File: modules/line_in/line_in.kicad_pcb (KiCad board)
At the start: 2 copper layers, 30.5 x 68.6 mm, 4 parts

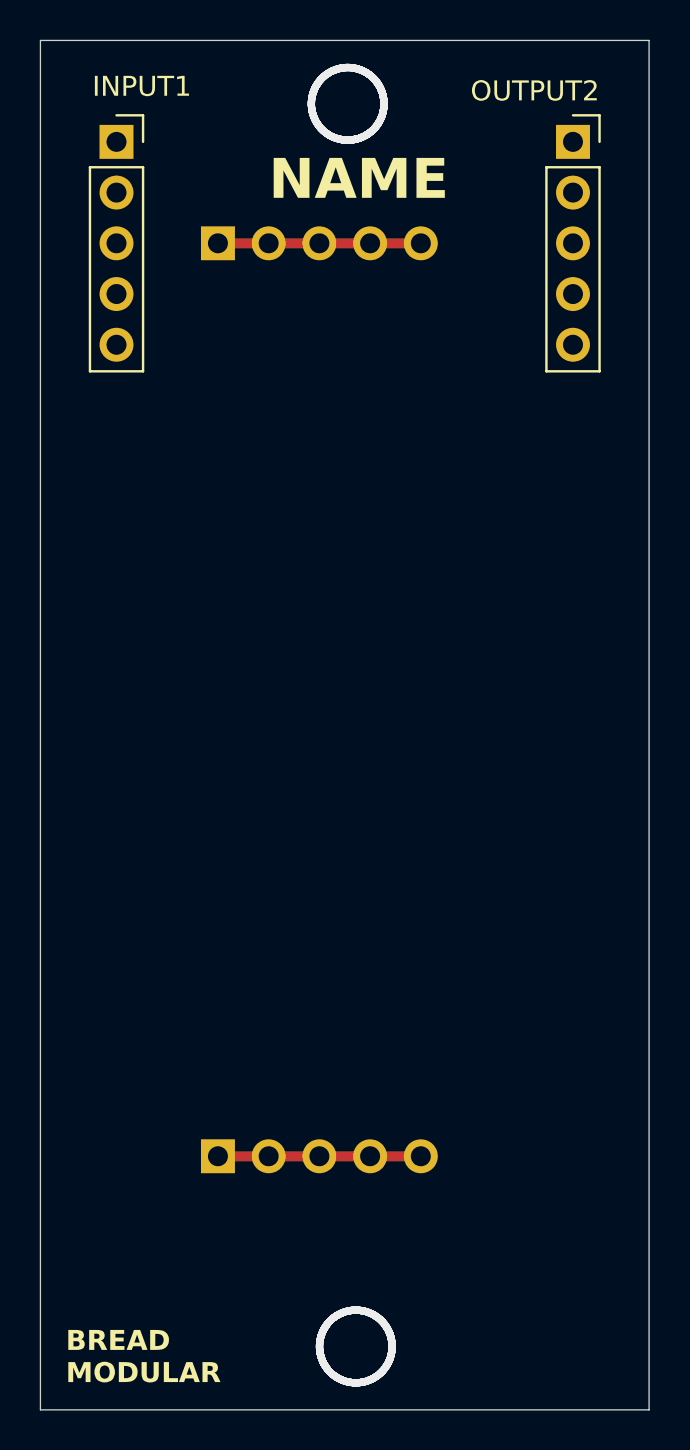
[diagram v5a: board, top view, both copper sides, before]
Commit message: Finished building the line_in module.
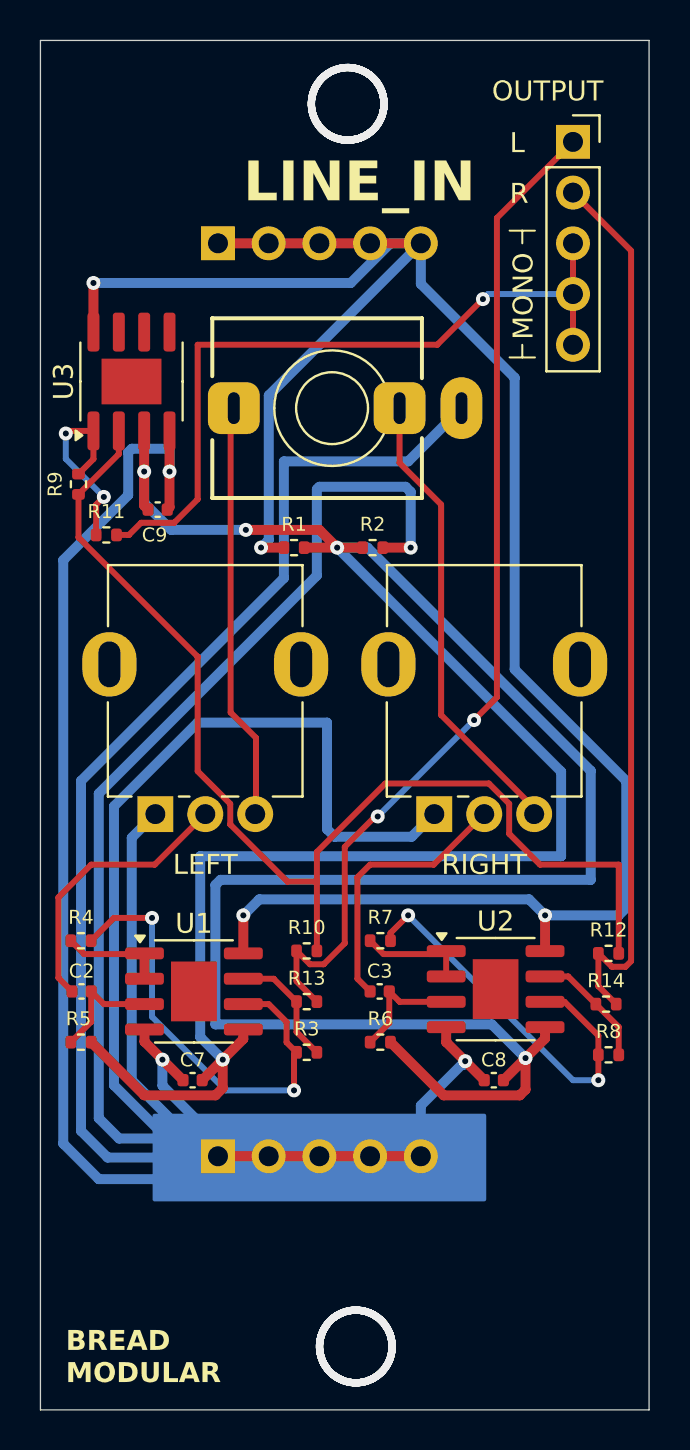
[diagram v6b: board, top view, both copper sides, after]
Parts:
- removed INPUT1: Conn_01x05_Socket, Connector_PinSocket_2.54mm:PinSocket_1x05_P2.54mm_Vertical
- added C2: 0.1uf, Capacitor_SMD:C_0402_1005Metric, F.Cu at (49.0, 88.3)
- added C3: 0.1uf, Capacitor_SMD:C_0402_1005Metric, F.Cu at (64.0, 88.3)
- added C7: 0.1uf, Capacitor_SMD:C_0402_1005Metric, F.Cu at (54.6, 92.7)
- added C8: 0.1uf, Capacitor_SMD:C_0402_1005Metric, F.Cu at (69.7, 92.7)
- added C9: 0.1uf, Capacitor_SMD:C_0402_1005Metric, F.Cu at (52.9, 64.1)
- added J1: AudioJack3, BreadModular_AudioJacks:Jack_3.5mm_QingPu_WQP-PJ366ST_Vertical, F.Cu at (61.6, 59.1)
- added LEFT: 50k, BreadModular_Pots:Potentiometer_RV09, F.Cu at (52.7, 79.4)
- added R1: 1k, Resistor_SMD:R_0402_1005Metric, F.Cu at (59.7, 66.0)
- added R10: 100k, Resistor_SMD:R_0402_1005Metric, F.Cu at (60.3, 86.2)
- added R11: 1k, Resistor_SMD:R_0402_1005Metric, F.Cu at (50.3, 65.4)
- added R12: 100k, Resistor_SMD:R_0402_1005Metric, F.Cu at (75.4, 86.4)
- added R13: 1k, Resistor_SMD:R_0402_1005Metric, F.Cu at (60.3, 88.8)
- added R14: 1k, Resistor_SMD:R_0402_1005Metric, F.Cu at (75.3, 88.9)
- added R2: 1k, Resistor_SMD:R_0402_1005Metric, F.Cu at (63.6, 66.0)
- added R3: 100k, Resistor_SMD:R_0402_1005Metric, F.Cu at (60.3, 91.3)
- added R4: 24k, Resistor_SMD:R_0402_1005Metric, F.Cu at (49.0, 85.7)
- added R5: 100k, Resistor_SMD:R_0402_1005Metric, F.Cu at (49.0, 90.8)
- added R6: 100k, Resistor_SMD:R_0402_1005Metric, F.Cu at (64.0, 90.8)
- added R7: 24k, Resistor_SMD:R_0402_1005Metric, F.Cu at (64.0, 85.7)
- added R8: 100k, Resistor_SMD:R_0402_1005Metric, F.Cu at (75.4, 91.4)
- added R9: 50k, Resistor_SMD:R_0402_1005Metric, F.Cu at (48.9, 62.9)
- added RIGHT: 50k, BreadModular_Pots:Potentiometer_RV09, F.Cu at (66.7, 79.4)
- added U1: TL072, Package_SO:SOIC-8-1EP_3.9x4.9mm_P1.27mm_EP2.29x3mm, F.Cu at (54.7, 88.3)
- added U2: TL072, Package_SO:SOIC-8-1EP_3.9x4.9mm_P1.27mm_EP2.29x3mm, F.Cu at (69.8, 88.2)
- added U3: TL072, Package_SO:SOIC-8-1EP_3.9x4.9mm_P1.27mm_EP2.29x3mm, F.Cu at (51.5, 57.7)
- renumbered OUTPUT2 to OUTPUT
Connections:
- net Net-(5V1-Pin_1) renamed +5V
- OUTPUT pad 1: unconnected-(OUTPUT2-Pin_1-Pad1) -> OUT_L
- OUTPUT pad 2: unconnected-(OUTPUT2-Pin_2-Pad2) -> OUT_R
- OUTPUT pad 3: unconnected-(OUTPUT2-Pin_3-Pad3) -> OUT_MONO
- OUTPUT pad 4: unconnected-(OUTPUT2-Pin_4-Pad4) -> OUT_MONO
- OUTPUT pad 5: unconnected-(OUTPUT2-Pin_5-Pad5) -> OUT_MONO
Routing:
- net GND: track 10.2 -> 251.7 mm, vias 0 -> 4
- net 2.5V: track 0.00 -> 158.6 mm, vias 0 -> 5
- net +5V: track 10.2 -> 110.8 mm, vias 0 -> 4
- net Net-(U3A--): track 0.00 -> 57.7 mm
- net OUT_L: track 0.00 -> 51.0 mm, vias 0 -> 2
- net OUT_R: track 0.00 -> 44.7 mm
- net OUT_MONO: track 0.00 -> 37.6 mm, vias 0 -> 1
- net Net-(U1B--): track 0.00 -> 23.3 mm, vias 0 -> 2
- net IN_R: track 0.00 -> 23.1 mm
- net IN_L: track 0.00 -> 20.9 mm
- net Net-(U2B--): track 0.00 -> 20.2 mm, vias 0 -> 2
- net Net-(C2-Pad1): track 0.00 -> 14.1 mm
- net Net-(C3-Pad1): track 0.00 -> 13.6 mm
- net Net-(R11-Pad1): track 0.00 -> 9.94 mm, vias 0 -> 2
- net Net-(R14-Pad1): track 0.00 -> 6.13 mm
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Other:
- board text added: "L"
- board text added: "LINE_IN"
- board text added: "MONO"
- board text added: "R"
- board text removed: "NAME"

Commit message: Add the line_in 0.3.0 production build
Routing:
- net Net-(U3A--): track 57.7 -> 58.3 mm
- net IN_L: track 20.9 -> 21.0 mm, vias 0 -> 1
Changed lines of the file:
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@@
 	)
 	(segment
-		(start 57.785 75.565)
-		(end 57.785 79.345)
-		(width 0.3)
-		(layer "F.Cu")
-		(net 10)
-	)
-	(segment
-		(start 56.515 74.295)
-		(end 57.785 75.565)
+		(start 56.515 74.041)
+		(end 56.515 76.073)
 		(width 0.3)
 		(layer "F.Cu")
@@
 	(segment
 		(start 56.515 59.215)
-		(end 56.515 74.295)
+		(end 56.515 74.041)
 		(width 0.3)
 		(layer "F.Cu")
@@
 		(net 10)
 	)
+	(via
+		(at 56.515 76.073)
+		(size 0.7)
+		(drill 0.3)
+		(layers "F.Cu" "B.Cu")
+		(net 10)
+	)
+	(segment
+		(start 56.515 78.155)
+		(end 57.745 79.385)
+		(width 0.3)
+		(layer "B.Cu")
+		(net 10)
+	)
+	(segment
+		(start 56.515 76.073)
+		(end 56.515 78.155)
+		(width 0.3)
+		(layer "B.Cu")
+		(net 10)
+	)
 	(segment
 		(start 76.57 51.17)
@@
 	)
 	(segment
-		(start 59.357233 82.765)
-		(end 60.835 82.765)
-		(width 0.3)
-		(layer "F.Cu")
-		(net 17)
-	)
-	(segment
 		(start 60.835 86.235)
 		(end 60.835 82.765)
@@
 	)
 	(segment
+		(start 59.944 80.387)
+		(end 59.944 77.089)
+		(width 0.5)
+		(layer "F.Cu")
+		(net 17)
+	)
+	(segment
 		(start 60.835 81.278)
 		(end 64.262 77.851)
@@
 	)
 	(segment
-		(start 54.864 71.498634)
-		(end 54.864 77.236233)
-		(width 0.3)
+		(start 48.895 65.671056)
+		(end 48.895 63.375)
+		(width 0.5)
 		(layer "F.Cu")
 		(net 17)
@@
 	)
 	(segment
-		(start 56.495 78.867233)
-		(end 56.495 79.902767)
-		(width 0.3)
-		(layer "F.Cu")
-		(net 17)
-	)
-	(segment
-		(start 54.864 77.236233)
-		(end 56.495 78.867233)
-		(width 0.3)
+		(start 54.61 70.866)
+		(end 49.919 66.175)
+		(width 0.5)
+		(layer "F.Cu")
+		(net 17)
+	)
+	(segment
+		(start 60.835 81.278)
+		(end 59.944 80.387)
+		(width 0.5)
+		(layer "F.Cu")
+		(net 17)
+	)
+	(segment
+		(start 55.372 77.089)
+		(end 54.61 76.327)
+		(width 0.5)
 		(layer "F.Cu")
 		(net 17)
@@
 	)
 	(segment
-		(start 48.895 65.529634)
-		(end 54.864 71.498634)
-		(width 0.3)
-		(layer "F.Cu")
-		(net 17)
-	)
-	(segment
-		(start 56.495 79.902767)
-		(end 59.357233 82.765)
-		(width 0.3)
+		(start 49.398944 66.175)
+		(end 48.895 65.671056)
+		(width 0.5)
+		(layer "F.Cu")
+		(net 17)
+	)
+	(segment
+		(start 49.919 66.175)
+		(end 49.398944 66.175)
+		(width 0.5)
 		(layer "F.Cu")
 		(net 17)
@@
 	)
 	(segment
-		(start 48.895 63.375)
-		(end 48.895 65.529634)
-		(width 0.3)
+		(start 54.61 76.327)
+		(end 54.61 70.866)
+		(width 0.5)
 		(layer "F.Cu")
 		(net 17)
@@
 		(layer "F.Cu")
 		(net 17)
+	)
+	(segment
+		(start 59.944 77.089)
+		(end 55.372 77.089)
+		(width 0.5)
+		(layer "F.Cu")
+		(net 17)

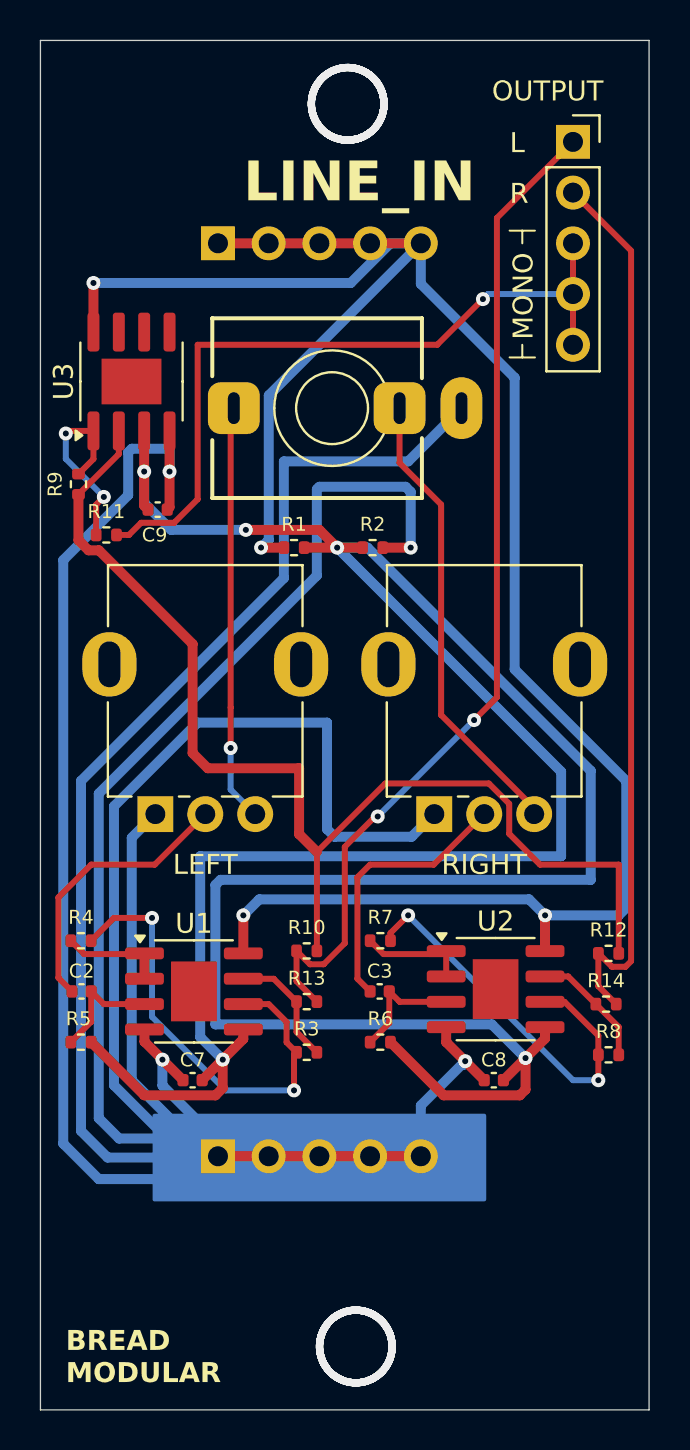
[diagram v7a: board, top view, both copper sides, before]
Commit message: Update line_in to use MCP6001 and 3V3.
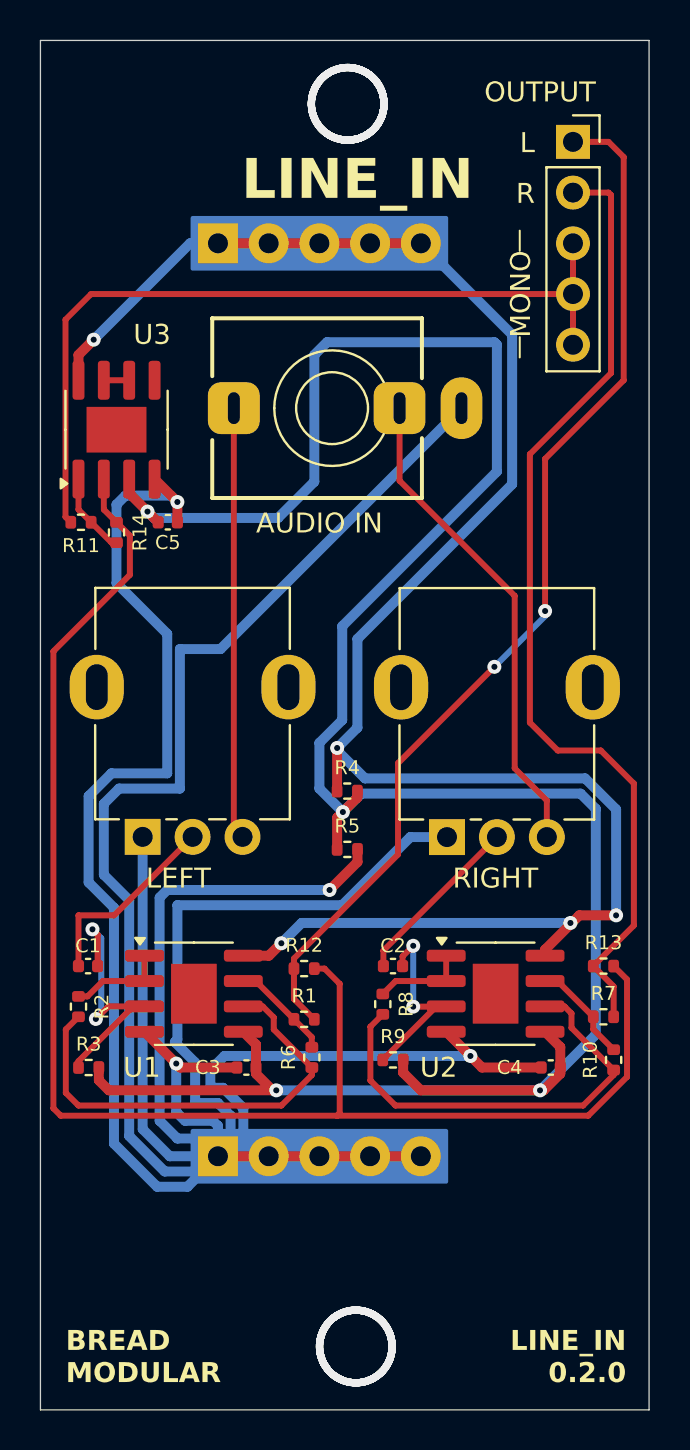
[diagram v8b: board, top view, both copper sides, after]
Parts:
- removed 5V1: Conn_01x05_Pin, Connector_PinHeader_2.54mm:PinHeader_1x05_P2.54mm_Vertical
- removed C7, C8, C9: 0.1uf, Capacitor_SMD:C_0402_1005Metric
- removed LEFT, RIGHT: 50k, BreadModular_Pots:Potentiometer_RV09
- removed OUTPUT: Conn_01x05_Socket, Connector_PinSocket_2.54mm:PinSocket_1x05_P2.54mm_Vertical
- added C1: 0.1uf, Capacitor_SMD:C_0402_1005Metric, F.Cu at (49.4, 87.0)
- added C4: 0.1uf, Capacitor_SMD:C_0402_1005Metric, F.Cu at (72.5, 92.1)
- added C5: 0.1uf, Capacitor_SMD:C_0402_1005Metric, F.Cu at (53.4, 64.8)
- added OUTPUT1: Conn_01x05_Socket, Connector_PinSocket_2.54mm:PinSocket_1x05_P2.54mm_Vertical, F.Cu at (73.7, 45.7)
- added RV1: 50k, BreadModular_Pots:Potentiometer_RV09, F.Cu at (52.1, 80.5)
- added RV2: 50k, BreadModular_Pots:Potentiometer_RV09, F.Cu at (67.3, 80.5)
- added VSUPPLY1: Conn_01x05_Pin, BreadModular_MISC:Power_Connector, B.Cu at (55.9, 50.8)
- GND1: footprint Connector_PinHeader_2.54mm:PinHeader_1x05_P2.54mm_Vertical -> BreadModular_MISC:Power_Connector
- R13: value 1k -> 100k
- R14: value 1k -> 50k
- R2: value 1k -> 24k
- R3: value 100k -> 1M
- R4, R7: value 24k -> 1k
- R5: value 100k -> 1k
- R8: value 100k -> 24k
- R9: value 50k -> 1M
- U1, U2, U3: value TL072 -> MCP6002-xSN
- moved R14 34.0 mm to (50.8, 65.3), turned to -90 degrees
- moved R9 32.9 mm to (64.6, 91.7), turned to 0 degrees
- moved R2 27.3 mm to (48.9, 89.0), turned to -90 degrees
- moved R1 23.6 mm to (60.2, 89.7)
- moved R5 16.5 mm to (62.4, 81.2)
- moved R10 16.3 mm to (75.7, 91.7), turned to 90 degrees
- moved C2 15.6 mm to (64.6, 87.0)
- moved R4 15.3 mm to (62.4, 78.2)
- moved R12 15.3 mm to (60.2, 87.1)
- moved R13 15.0 mm to (75.2, 87.0)
- moved R7 11.8 mm to (75.2, 89.5)
- moved R8 11.6 mm to (64.1, 88.9), turned to -90 degrees
- moved R3 10.9 mm to (49.4, 92.1)
- moved C3 7.69 mm to (57.3, 92.1)
- moved R6 3.51 mm to (60.6, 91.6), turned to 90 degrees
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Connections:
- C2 pad 2: Net-(U1A-+) -> Net-(U2A-+)
- C3 pad 1: Net-(C3-Pad1) -> GND
- C3 pad 2: Net-(U2A-+) -> V_MID
- R1 pad 1: +5V -> Net-(R1-Pad1)
- R1 pad 2: 2.5V -> OUT_L
- R10 pad 1: OUT_L -> Net-(U2B--)
- R10 pad 2: Net-(U3A--) -> Net-(R10-Pad2)
- R12 pad 1: OUT_R -> OUT_L
- R13 pad 1: Net-(R13-Pad1) -> OUT_R
- R13 pad 2: OUT_L -> Net-(U3A--)
- R14 pad 1: Net-(R14-Pad1) -> Net-(U3A--)
- R14 pad 2: OUT_R -> Net-(R11-Pad1)
- R2 pad 1: 2.5V -> Net-(U1A--)
- R2 pad 2: GND -> Net-(U1B--)
- R3 pad 1: Net-(U1B--) -> Net-(U1A-+)
- R3 pad 2: Net-(R13-Pad1) -> V_MID
- R4 pad 1: Net-(U1A--) -> V_SUPLY
- R4 pad 2: Net-(U1B--) -> V_MID
- R5 pad 1: Net-(U1A-+) -> V_MID
- R5 pad 2: 2.5V -> GND
- R6 pad 1: Net-(U2A-+) -> Net-(U1B--)
- R6 pad 2: 2.5V -> Net-(R1-Pad1)
- R7 pad 1: Net-(U2A--) -> Net-(R10-Pad2)
- R7 pad 2: Net-(U2B--) -> OUT_R
- R8 pad 1: Net-(U2B--) -> Net-(U2A--)
- R8 pad 2: Net-(R14-Pad1) -> Net-(U2B--)
- R9 pad 1: Net-(U3A--) -> Net-(U2A-+)
- R9 pad 2: Net-(R11-Pad1) -> V_MID
- U1 pad 5: 2.5V -> V_MID
- U1 pad 7: Net-(R13-Pad1) -> Net-(R1-Pad1)
- U1 pad 8: +5V -> V_SUPLY
- U2 pad 5: 2.5V -> V_MID
- U2 pad 7: Net-(R14-Pad1) -> Net-(R10-Pad2)
- U2 pad 8: +5V -> V_SUPLY
- U3 pad 3: 2.5V -> V_MID
- U3 pad 6: unconnected-(U3B---Pad6) -> Net-(U3B--)
- U3 pad 7: unconnected-(U3-Pad7) -> Net-(U3B--)
- U3 pad 8: +5V -> V_SUPLY
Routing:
- net 2.5V: track 158.6 -> 0.00 mm, vias 5 -> 0
- net V_MID: track 0.00 -> 125.6 mm, vias 0 -> 4
- net +5V: track 110.8 -> 0.00 mm, vias 4 -> 0
- net V_SUPLY: track 0.00 -> 95.9 mm, vias 0 -> 5
- net GND: track 251.7 -> 224.1 mm
- net Net-(U3A--): track 58.3 -> 77.4 mm
- net Net-(C3-Pad1): track 13.6 -> 0.00 mm
- net Net-(C1-Pad1): track 0.00 -> 9.88 mm
- net Net-(U1A-+): track 5.90 -> 14.2 mm, vias 0 -> 2
- net Net-(R14-Pad1): track 6.13 -> 0.00 mm
- net Net-(R13-Pad1): track 6.10 -> 0.00 mm
- net Net-(R11-Pad1): track 9.94 -> 4.12 mm, vias 2 -> 0
- net Net-(C2-Pad1): track 14.1 -> 8.81 mm
- net Net-(R10-Pad2): track 0.00 -> 5.23 mm
- net Net-(R1-Pad1): track 0.00 -> 5.10 mm
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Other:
- board text added: "AUDIO IN"
- board text added: "LEFT"
- board text added: "LINE_IN 0.2.0"
- board text added: "OUTPUT"
- board text added: "RIGHT"
